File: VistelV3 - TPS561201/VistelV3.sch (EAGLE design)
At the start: 191 parts, among them IC1 LD117ADT33TR, IC5 SI7006-A10-IM, J2 RJ45-ABRACON-11108B, J3 RJ45-ABRACON-11108B, K1 ZF112, K2 ZF112, K3 ZF112, K4 ZF112, T1 MOSFET-NCHANNELBSS123LT1G, T2 MOSFET-NCHANNELBSS123LT1G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

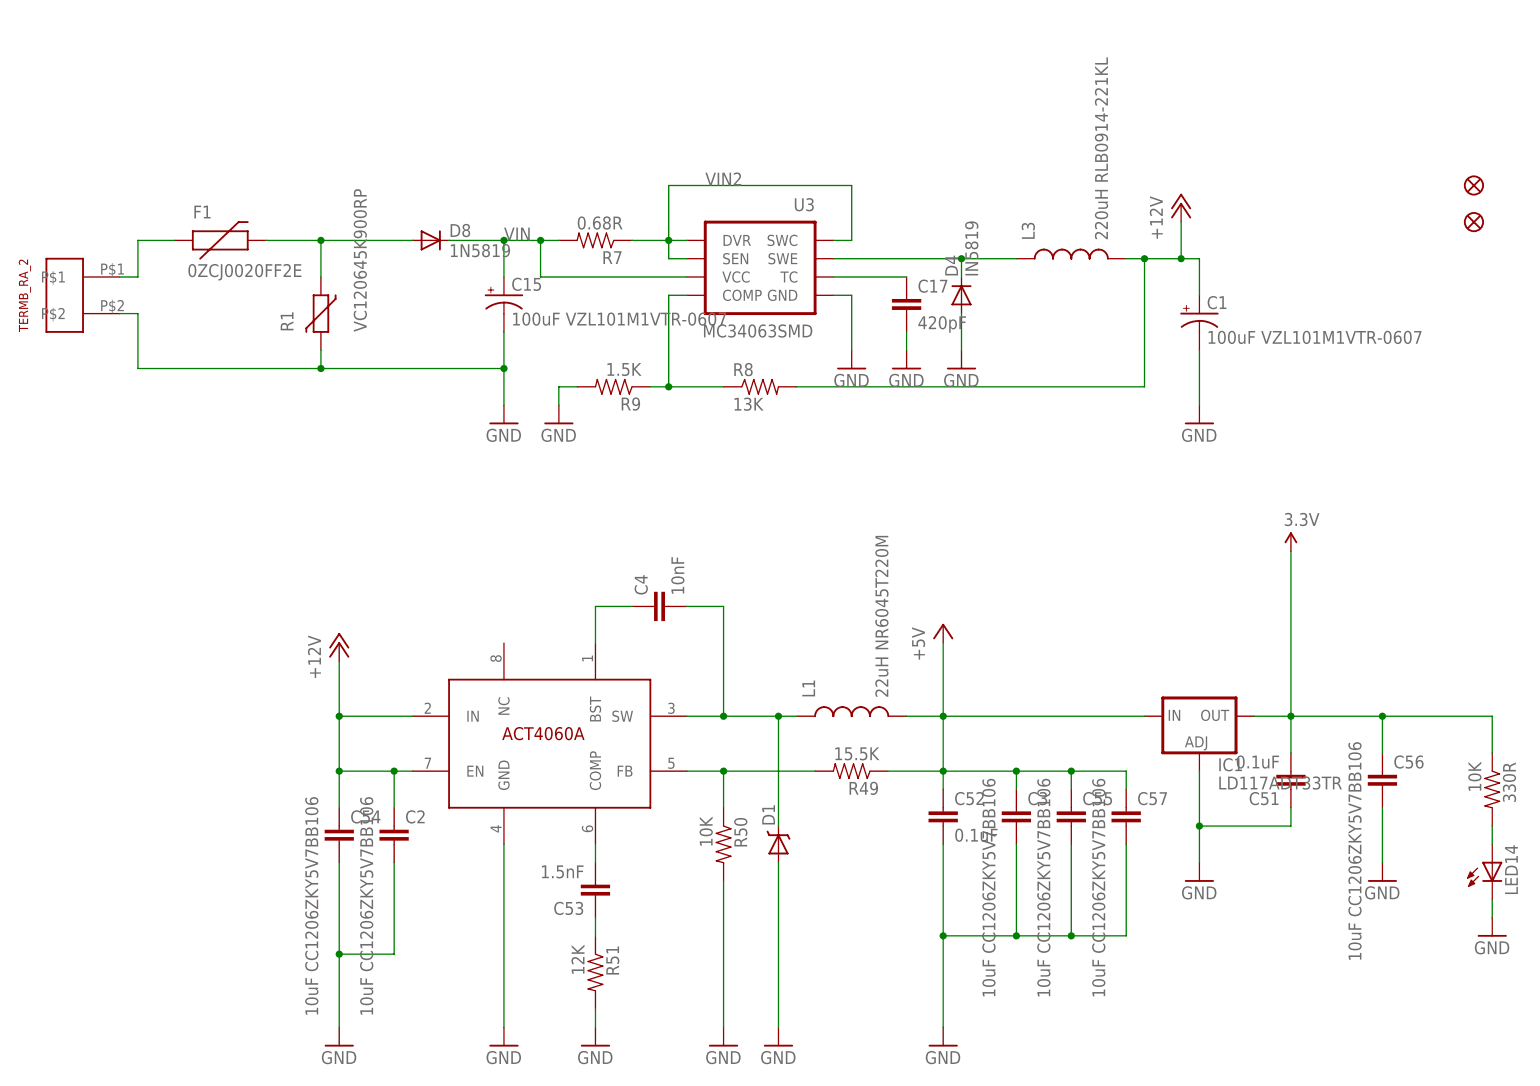
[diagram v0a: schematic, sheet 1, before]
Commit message: Updated Power suply section
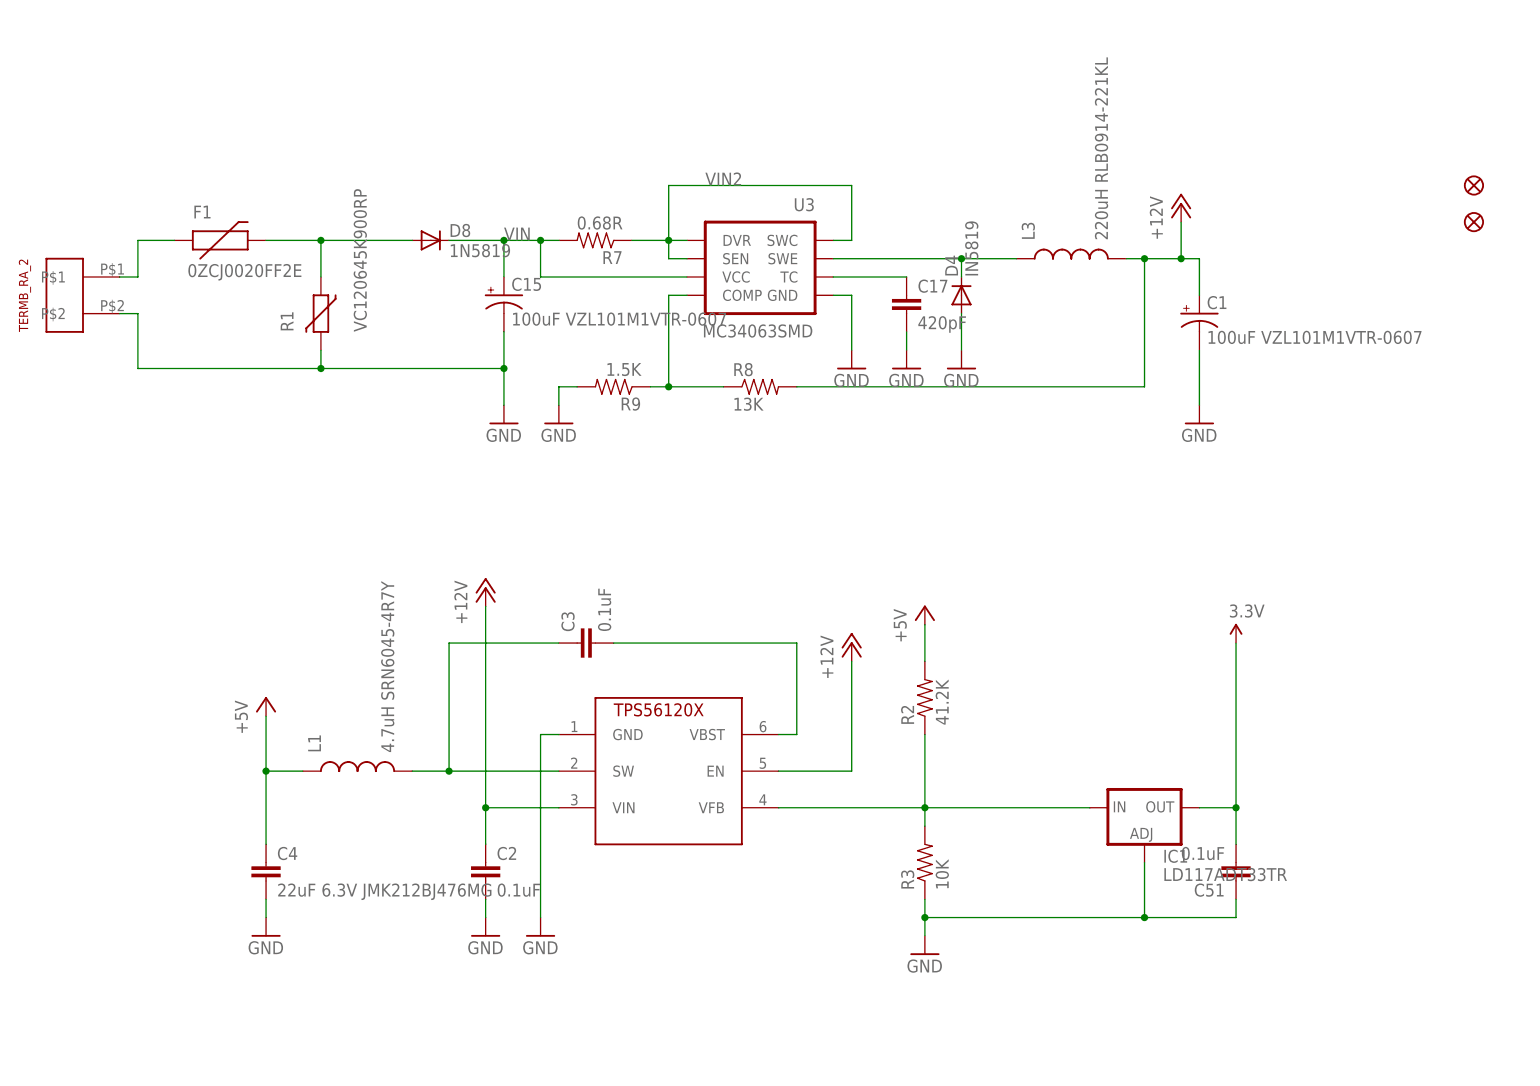
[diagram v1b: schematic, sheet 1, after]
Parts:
- removed 330R, R50: 10K, SparkFun-Passives:RESISTOR0805-RES
- removed C52: 0.1uF, SparkFun-Passives:CAP0805
- removed C53: 1.5nF, SparkFun-Passives:CAP0805
- removed C54, C55, C56, C57: 10uF CC1206ZKY5V7BB106, SparkFun-Passives:CAP1206
- removed D1: (no value), SparkFun-DiscreteSemi:B340A
- removed LED14: (no value), SparkFun-LED:LED-FKIT-1206
- removed R49: 15.5K, SparkFun-Passives:RESISTOR0805-RES
- removed R51: 12K, SparkFun-Passives:RESISTOR0805-RES
- added R2: 41.2K, SparkFun-Passives:RESISTOR0805-RES
- added R3: 10K, SparkFun-Passives:RESISTOR0805-RES
- C2, C3: value 10uF CC1206ZKY5V7BB106 -> 0.1uF; device SparkFun-Passives:CAP1206 -> SparkFun-Passives:CAP0805
- C4: value 10nF -> 22uF 6.3V JMK212BJ476MG
- L1: value 22uH NR6045T220M -> 4.7uH SRN6045-4R7Y; device SparkFun-Passives:INDUCTOR -> SparkFun-Passives:INDUCTOR0805
- U$18: value ACT4060A -> (none); device VistelV3:ACT4060A -> VistelV3:TPS56120X
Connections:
- removed net N$18: C4.2, D1.C, L1.1, U$18.SW
- removed net N$23: C53.2, U$18.COMP
- removed net N$32: C53.1, R51.1
- net +12V: now also U$18.VIN; no longer C54.1, U$18.IN
- net +5V: now also C4.1, L1.1, R2.2; no longer C3.1, C52.1, C55.1, C57.1, IC1.IN, L1.2, R49.1
- net 3.3V: no longer 330R.1, C56.1
- net GND: now also C4.2, R3.1; no longer C3.2, C52.2, C54.2, C55.2, C56.2, C57.2, D1.A, LED14.C, R50.2, R51.2
- net N$19: now also C3.2, U$18.VBST; no longer R49.2, R50.1, U$18.FB
- net N$20: now also IC1.IN, R2.1, R3.2, U$18.VFB; no longer 330R.2, LED14.A
- net N$6: now also C3.1, L1.2, U$18.SW; no longer C4.1, U$18.BST
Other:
- moved on the sheet: C2, C3, C4, C51, IC1, L1
